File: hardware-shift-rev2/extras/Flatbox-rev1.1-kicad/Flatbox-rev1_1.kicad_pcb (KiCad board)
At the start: 2 copper layers, 227.1 x 120 mm, 26 parts, among them SW1 SW_Push, SW10 SW_Push, SW11 SW_Push, SW12 SW_Push, SW13 SW_Push, SW14 SW_Push, SW15 SW_Push, SW16 SW_Push, SW17 SW_Push, SW18 SW_Push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

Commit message: minimal changes should work 100% because i changed literally nothing
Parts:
- added REF**: MountingHole_6.4mm_M6, MountingHole:MountingHole_6.4mm_M6, F.Cu at (133.5, 78.0)
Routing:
- net GND: track 0.00 -> 763.1 mm
- net OPT1: track 0.00 -> 173.2 mm
- net L2: track 0.00 -> 170.9 mm
- net R2: track 0.00 -> 140.5 mm
- net L1: track 0.00 -> 139.9 mm
- net UP: track 0.00 -> 124.6 mm
- net R1: track 0.00 -> 111.2 mm
- net CIRCLE: track 0.00 -> 98.7 mm
- net LEFT: track 0.00 -> 96.2 mm
- net CROSS: track 0.00 -> 80.5 mm
- net RIGHT: track 0.00 -> 67.1 mm
- net TRIANGLE: track 0.00 -> 65.5 mm
- net OPT2: track 0.00 -> 62.1 mm
- net DOWN: track 0.00 -> 55.7 mm
- net OPT3: track 0.00 -> 52.5 mm
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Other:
- board text added: "Shiftbox"
- board text added: "circle"
- board text added: "cross"
- board text added: "down"
- board text added: "github.com/xpire/flatbox-shift"
- board text added: "l1"
- board text added: "l2"
- board text added: "left"
- board text added: "r1"
- board text added: "r2"
- board text added: "right"
- board text added: "shift"
- board text added: "square"
- board text added: "triangle"
- board text removed: "Flatbox"
- board text removed: "github.com/jfedor2/flatbox"

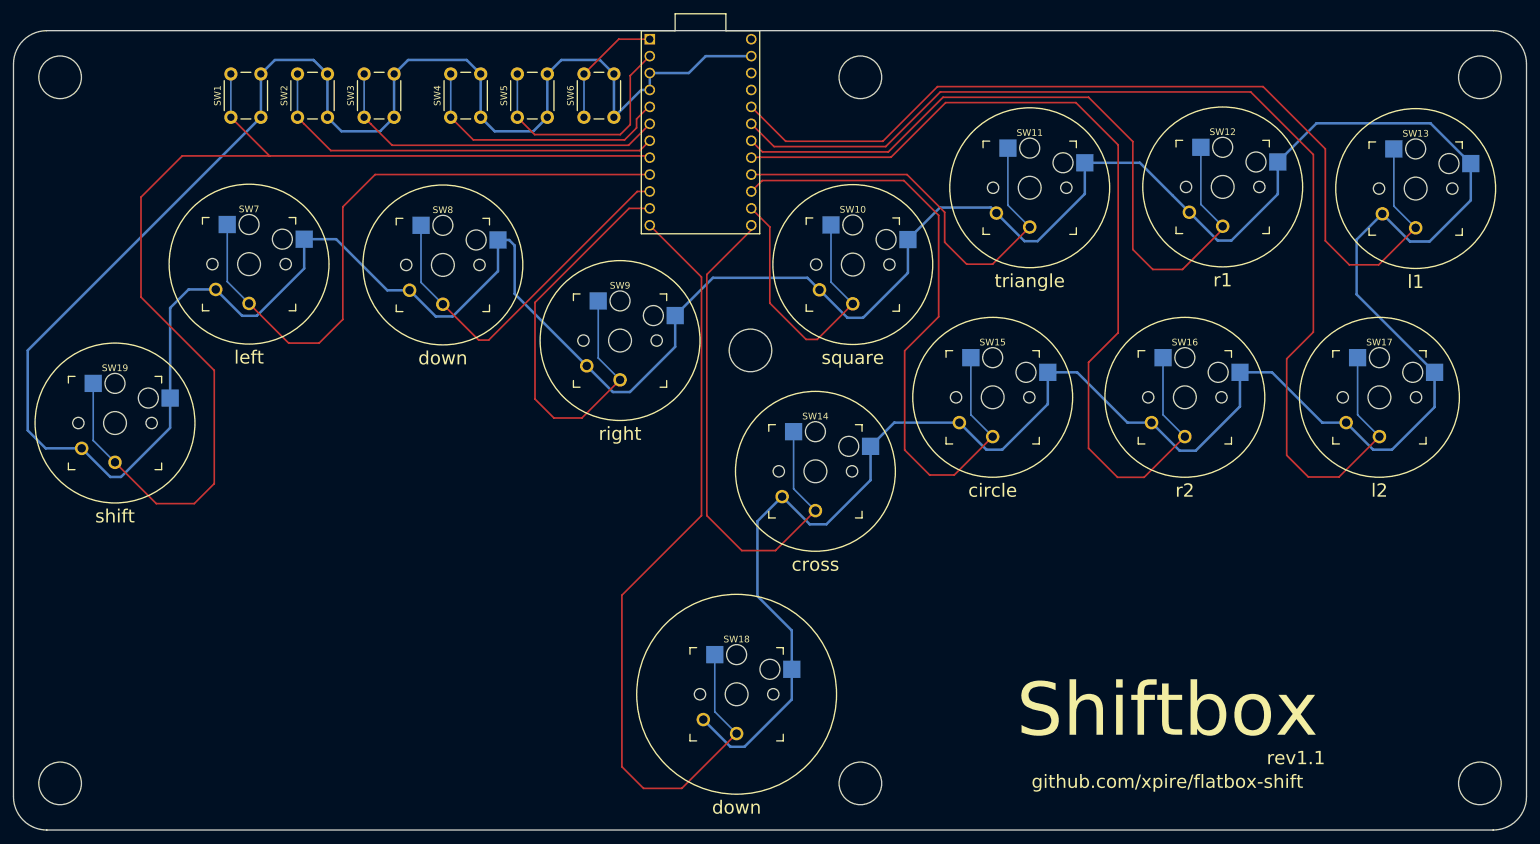
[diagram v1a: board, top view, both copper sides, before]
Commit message: finalised MX compatiable hotswap pcb
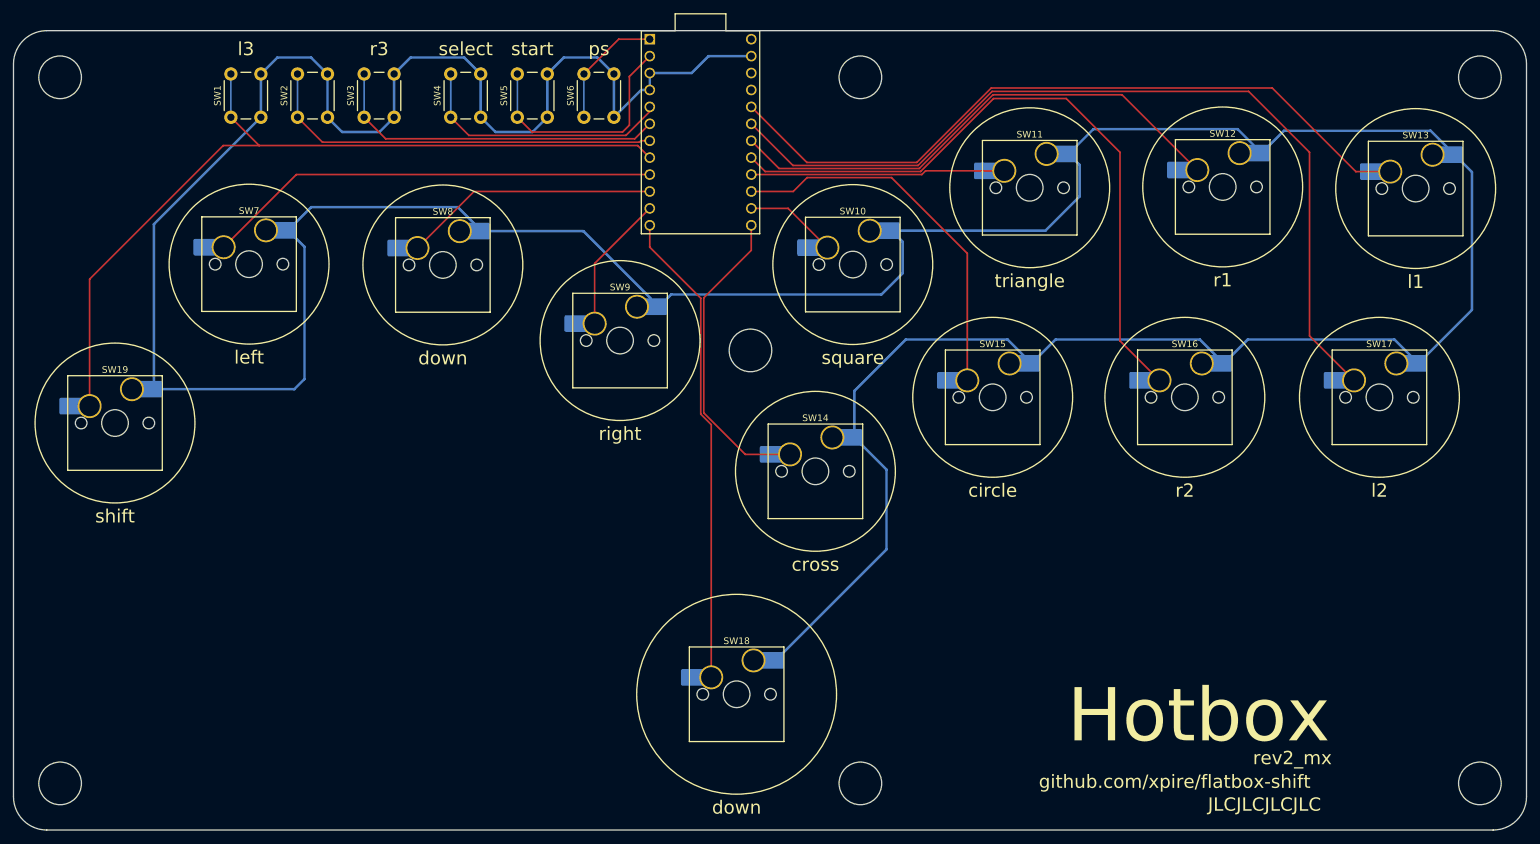
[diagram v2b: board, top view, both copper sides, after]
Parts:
- SW10, SW11, SW12, SW13, SW14, SW15, SW16, SW17, SW18, SW19, SW7, SW8, SW9: footprint Kailh:Kailh_socket_PG1350_optional -> Switch_Keyboard_Hotswap_Kailh:SW_Hotswap_Kailh_MX_plated_1.00u
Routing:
- net GND: track 763.1 -> 612.5 mm
- net UP: track 124.6 -> 71.7 mm
- net OPT1: track 173.2 -> 124.7 mm
- net RIGHT: track 67.1 -> 20.7 mm
- net CIRCLE: track 98.7 -> 57.1 mm
- net R2: track 140.5 -> 100.8 mm
- net L2: track 170.9 -> 131.8 mm
- net CROSS: track 80.5 -> 46.6 mm
- net SQUARE: track 45.5 -> 13.9 mm
- net R1: track 111.2 -> 80.7 mm
- net L1: track 139.9 -> 112.0 mm
- net TRIANGLE: track 65.5 -> 38.2 mm
- net LEFT: track 96.2 -> 71.3 mm
- net DOWN: track 55.7 -> 41.2 mm
- net OPT2: track 62.1 -> 61.0 mm
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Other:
- board text added: "Hotbox"
- board text added: "JLCJLCJLCJLC"
- board text added: "l3"
- board text added: "ps"
- board text added: "r3"
- board text added: "rev2_mx"
- board text added: "select"
- board text added: "start"
- board text removed: "Shiftbox"
- board text removed: "rev1.1"
